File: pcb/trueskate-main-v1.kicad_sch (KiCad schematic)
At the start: 0 parts

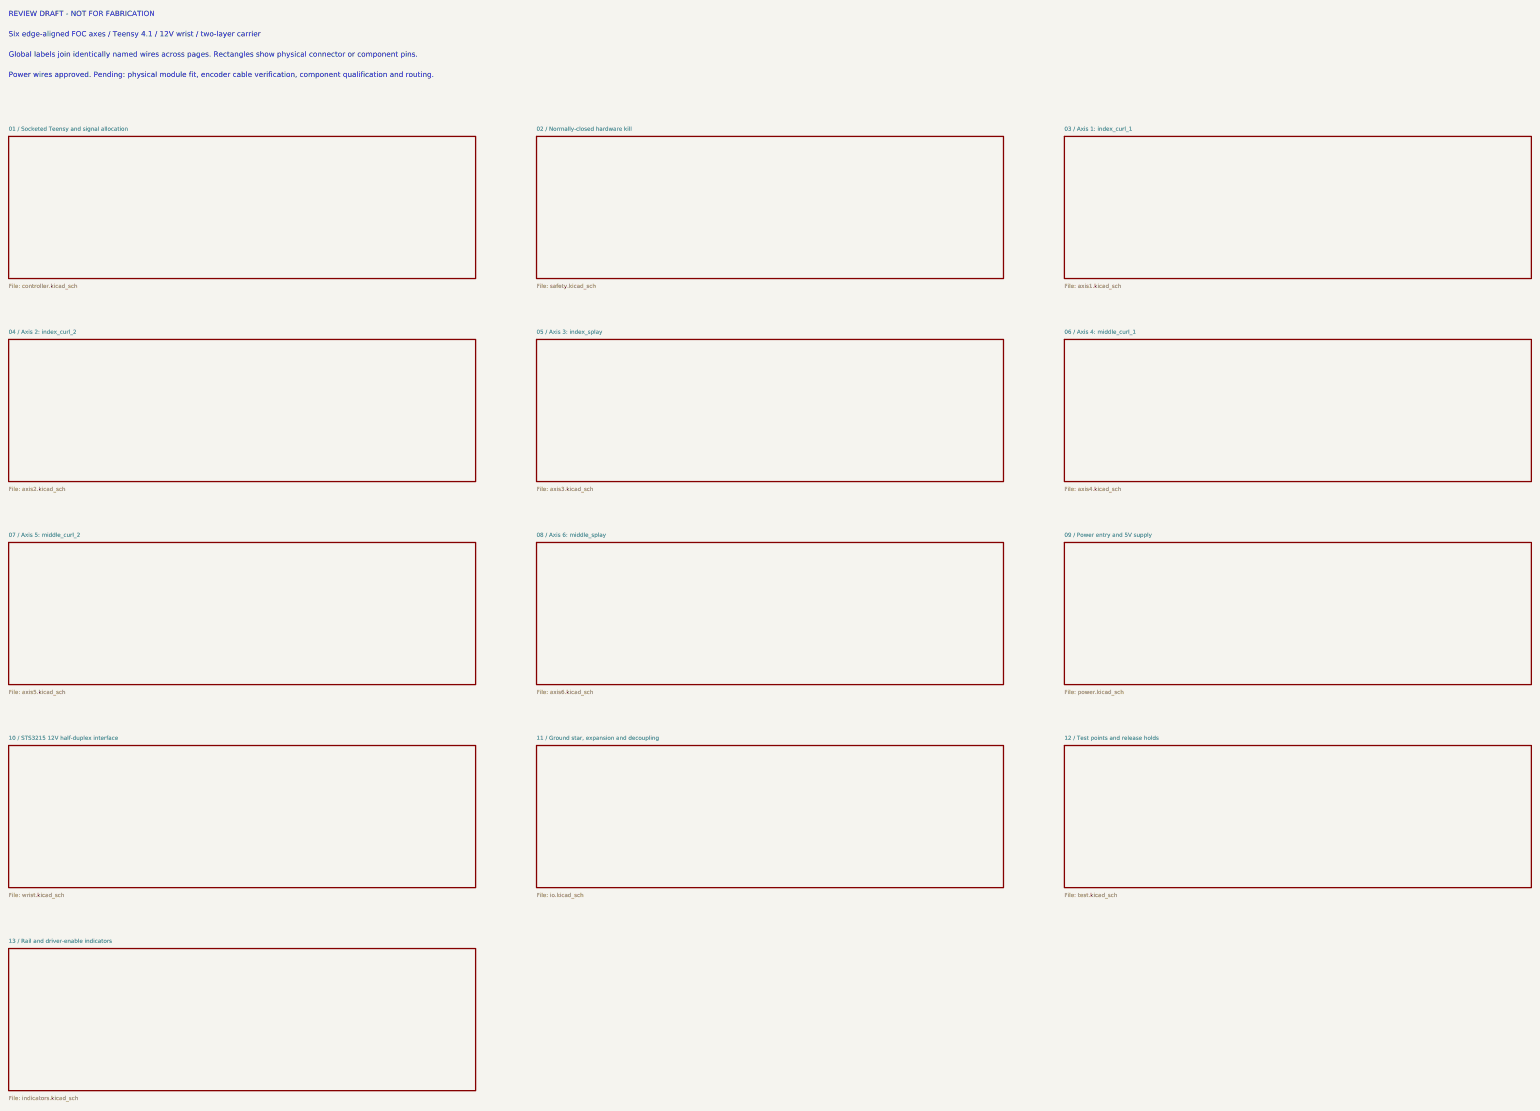
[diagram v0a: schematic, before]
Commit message: feat: finish through-hole six-axis carrier review design
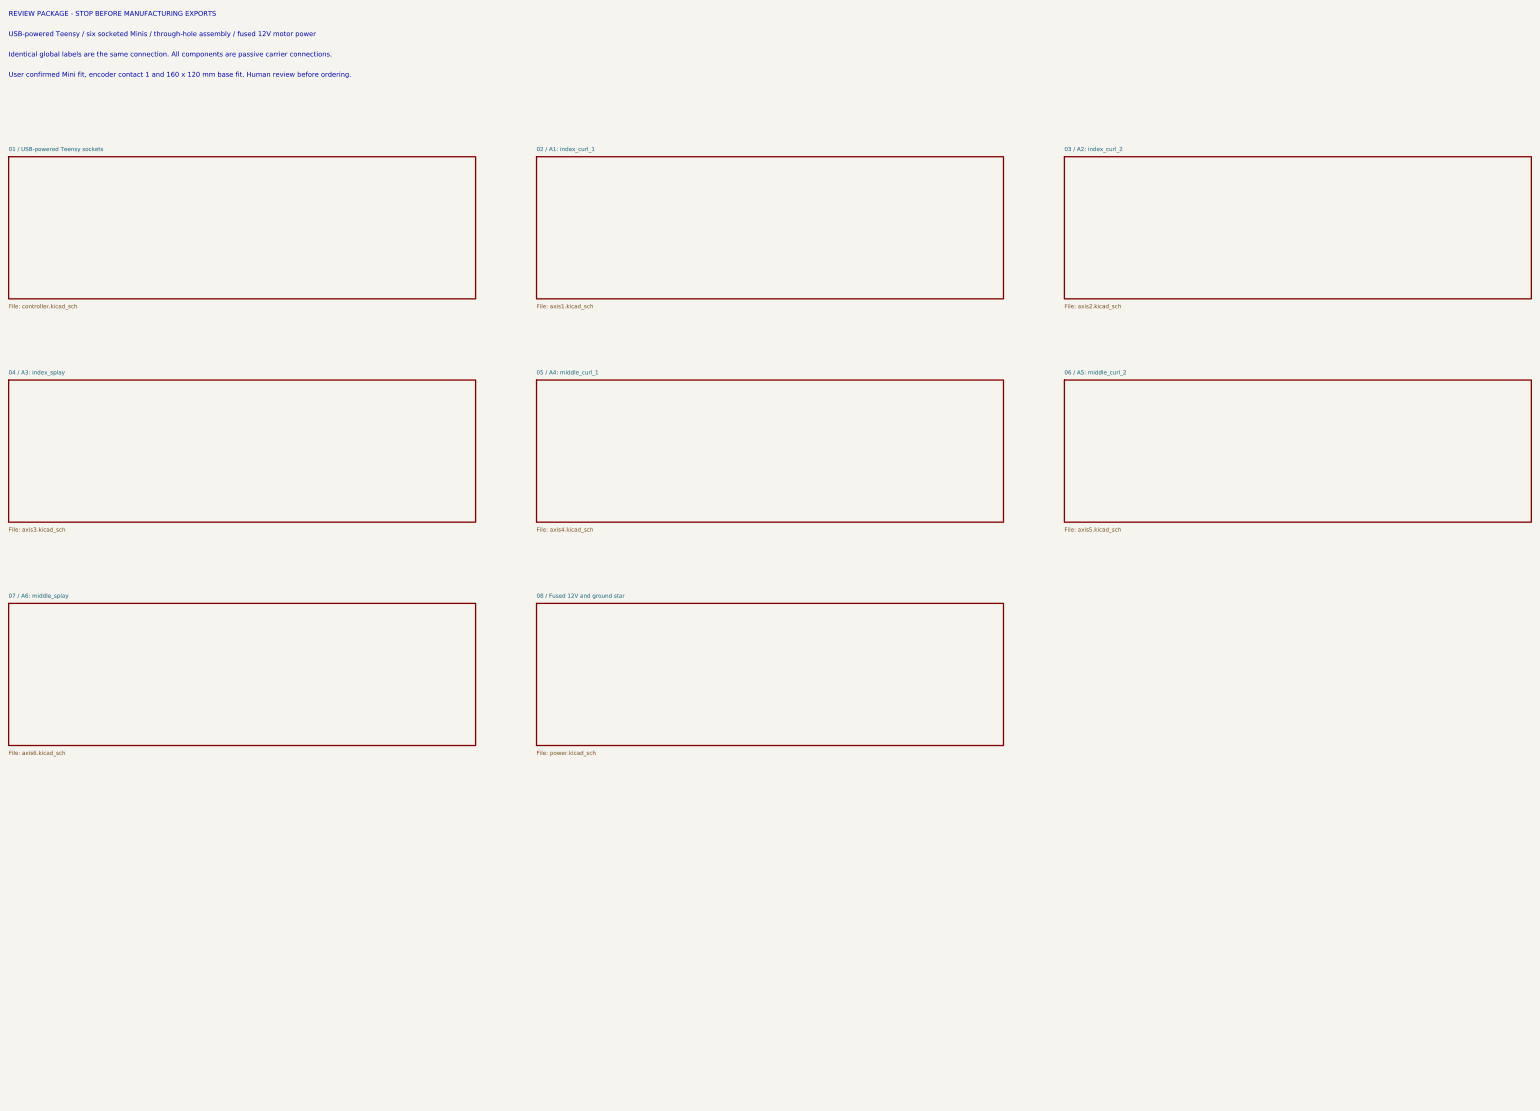
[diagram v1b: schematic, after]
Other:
- sheet 01 / Socketed Teensy and signal allocation renamed 01 / USB-powered Teensy sockets
- sheet 03 / Axis 1: index_curl_1 renamed 02 / A1: index_curl_1
- sheet 04 / Axis 2: index_curl_2 renamed 03 / A2: index_curl_2
- sheet 05 / Axis 3: index_splay renamed 04 / A3: index_splay
- sheet 06 / Axis 4: middle_curl_1 renamed 05 / A4: middle_curl_1
- sheet 07 / Axis 5: middle_curl_2 renamed 06 / A5: middle_curl_2
- sheet 08 / Axis 6: middle_splay renamed 07 / A6: middle_splay
- sheet 09 / Power entry and 5V supply renamed 08 / Fused 12V and ground star
- removed sheet 02 / Normally-closed hardware kill
- removed sheet 10 / STS3215 12V half-duplex interface
- removed sheet 11 / Ground star, expansion and decoupling
- removed sheet 12 / Test points and release holds
- removed sheet 13 / Rail and driver-enable indicators
- note added: "Identical global labels are the same connection. All components are passive carrier connections."
- note added: "REVIEW PACKAGE - STOP BEFORE MANUFACTURING EXPORTS"
- note added: "USB-powered Teensy / six socketed Minis / through-hole assembly / fused 12V motor power"
- note added: "User confirmed Mini fit, encoder contact 1 and 160 x 120 mm base fit. Human review before ordering."
- note removed: "Global labels join identically named wires across pages. Rectangles show physical connector or component pins."
- note removed: "Power wires approved. Pending: physical module fit, encoder cable verification, component qualification and routing."
- note removed: "REVIEW DRAFT - NOT FOR FABRICATION"
- note removed: "Six edge-aligned FOC axes / Teensy 4.1 / 12V wrist / two-layer carrier"
- title: TrueSkate main control PCB -> TrueSkate USB-powered six-axis carrier

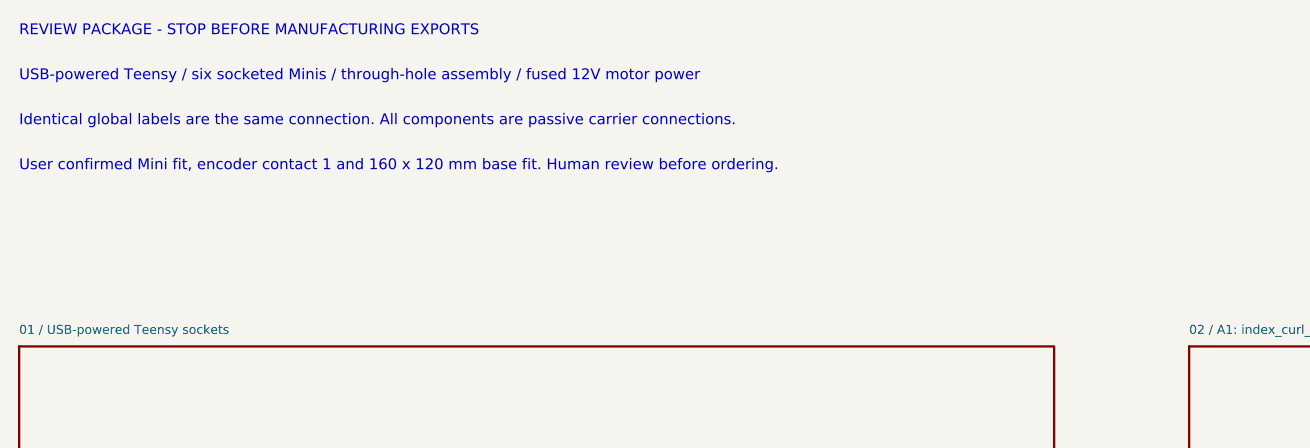
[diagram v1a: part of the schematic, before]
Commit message: feat: use exact Mini v1.0 footprints with direct power routing
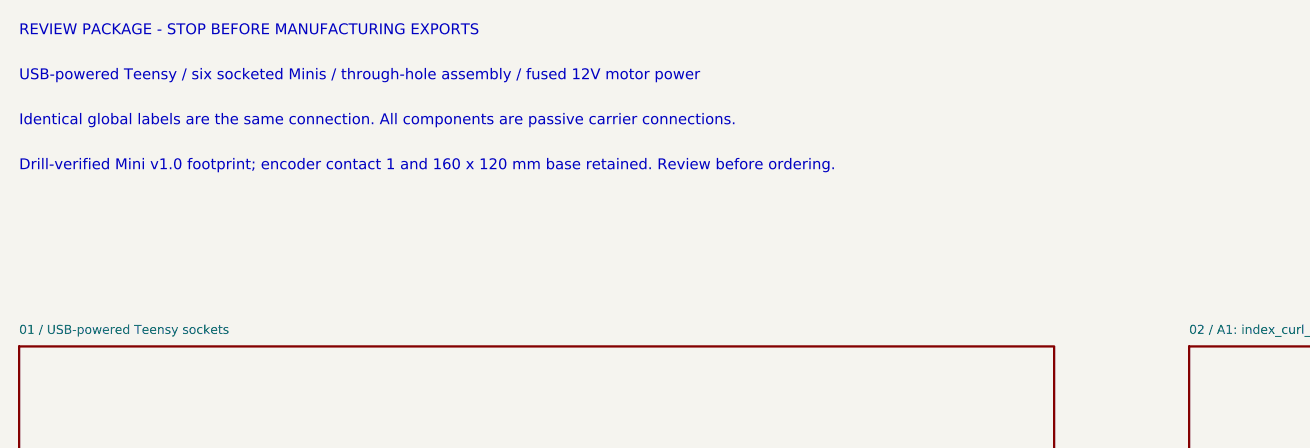
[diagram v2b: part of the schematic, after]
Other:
- note added: "Drill-verified Mini v1.0 footprint; encoder contact 1 and 160 x 120 mm base retained. Review before ordering."
- note removed: "User confirmed Mini fit, encoder contact 1 and 160 x 120 mm base fit. Human review before ordering."

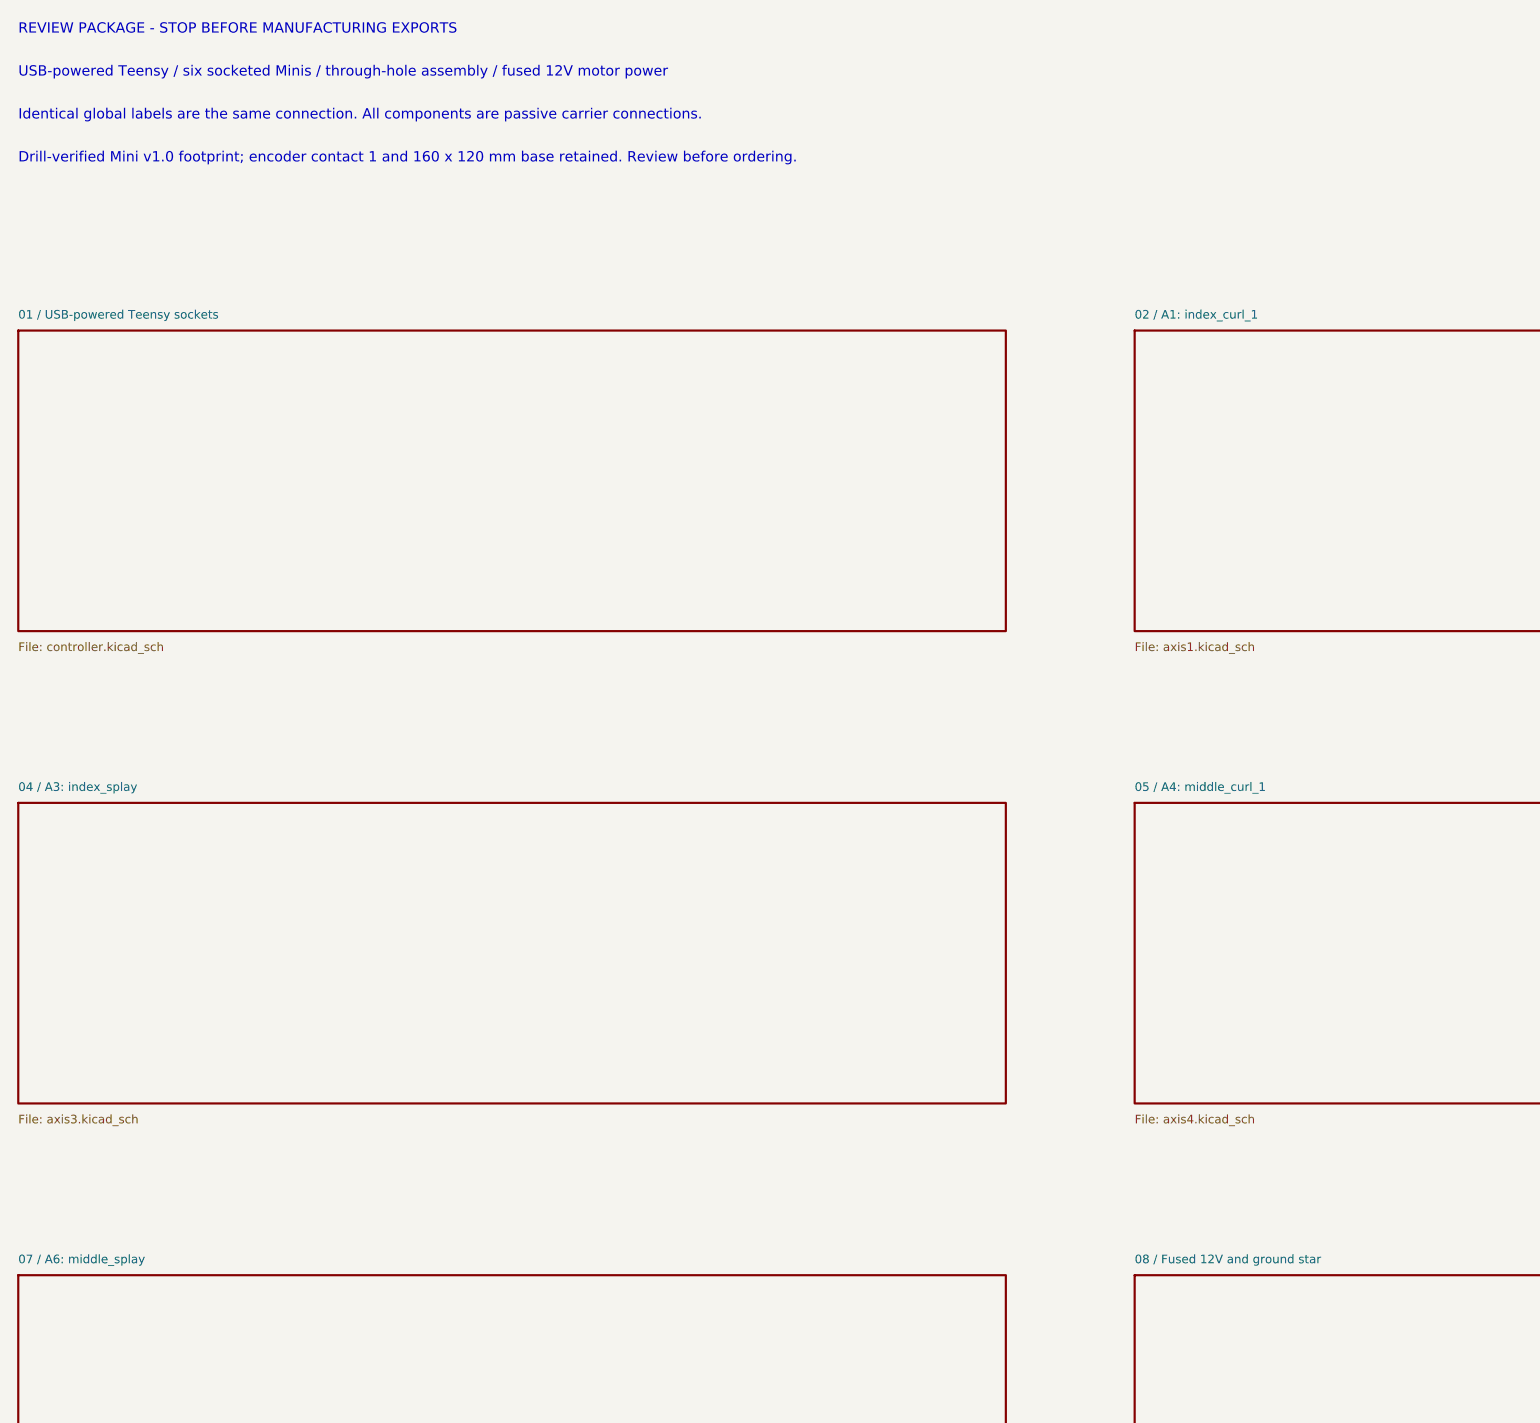
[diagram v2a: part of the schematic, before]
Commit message: feat: relayout carrier with edge connectors and hardware kill
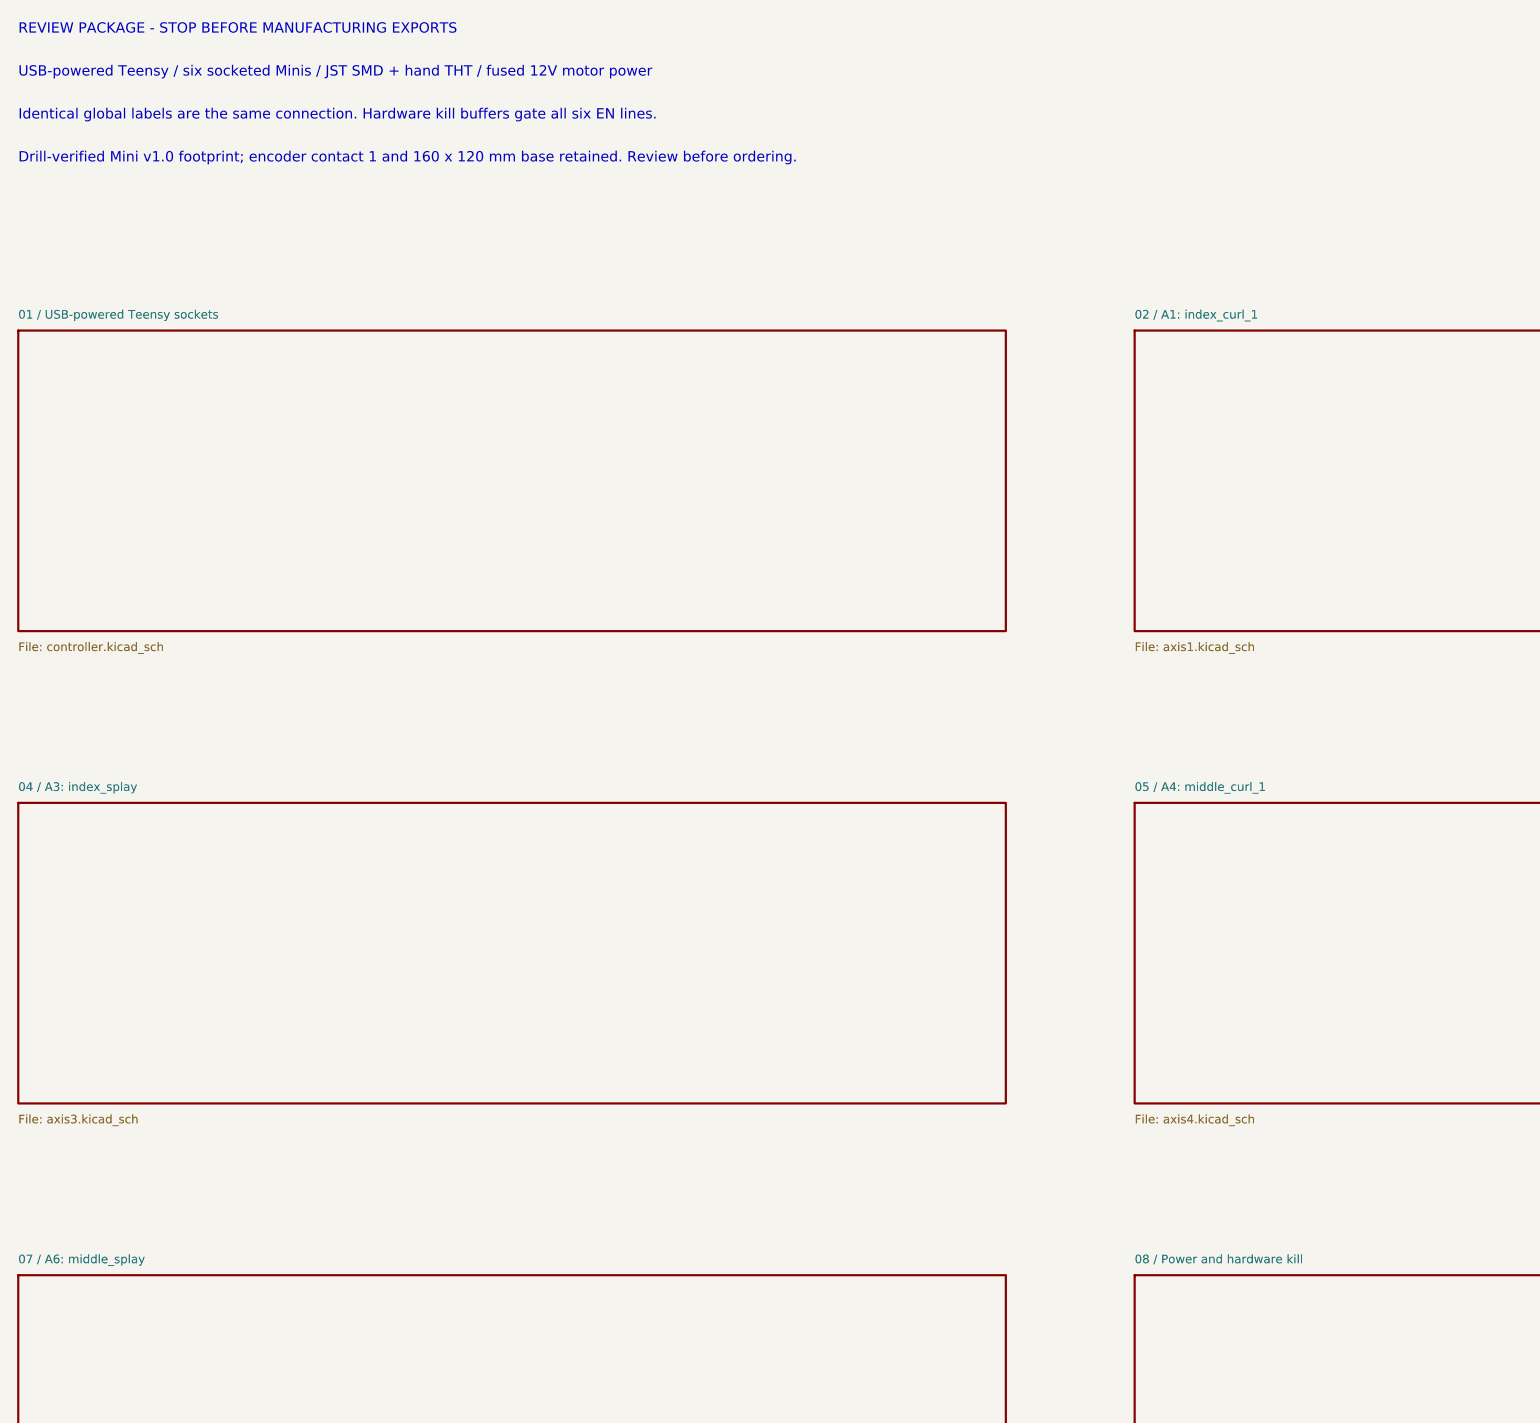
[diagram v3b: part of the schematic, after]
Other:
- sheet 08 / Fused 12V and ground star renamed 08 / Power and hardware kill
- note added: "Identical global labels are the same connection. Hardware kill buffers gate all six EN lines."
- note added: "USB-powered Teensy / six socketed Minis / JST SMD + hand THT / fused 12V motor power"
- note removed: "Identical global labels are the same connection. All components are passive carrier connections."
- note removed: "USB-powered Teensy / six socketed Minis / through-hole assembly / fused 12V motor power"
